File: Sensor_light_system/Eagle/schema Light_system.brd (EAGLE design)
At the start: 80.1 x 49.8 mm, 17 parts, among them IC1 STM32F030C8T6TR, J1 12_WAY_CON

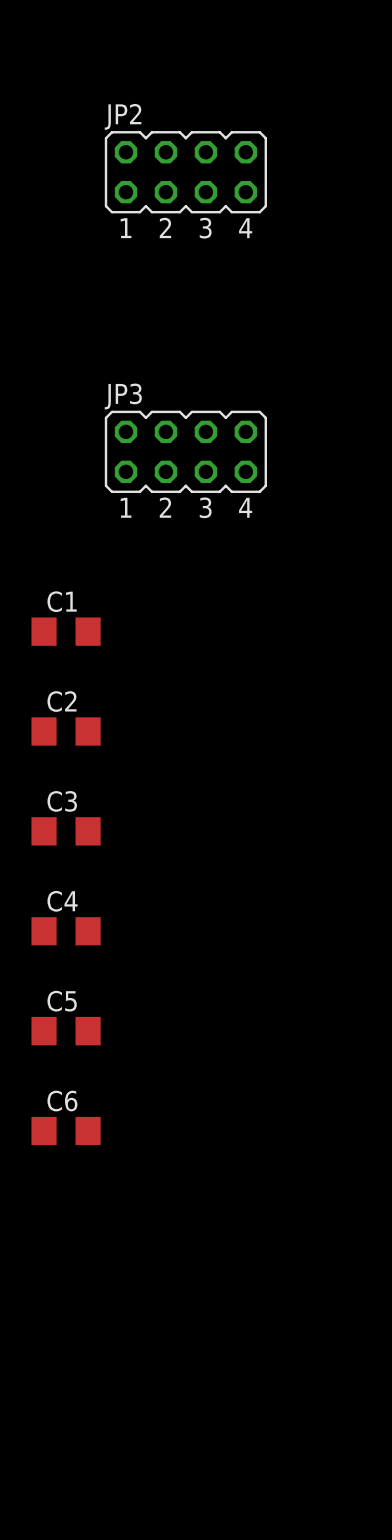
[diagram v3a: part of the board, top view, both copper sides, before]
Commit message: schema sensor gewijzigd
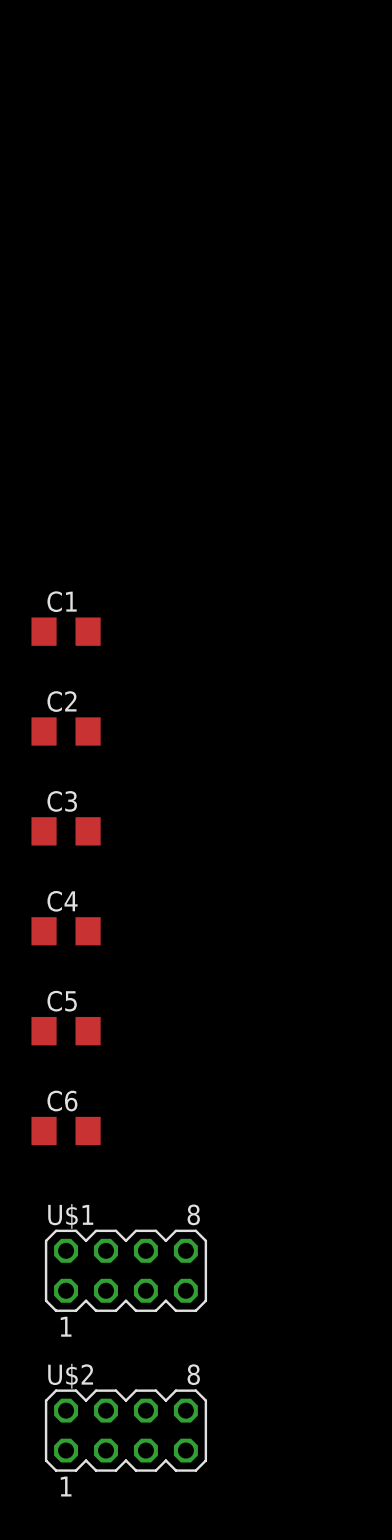
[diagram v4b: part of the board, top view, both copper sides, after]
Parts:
- removed JP2, JP3: (no value), jumper:JP4Q
- added U$1, U$2: MODULARCONNECTOR, Main_lib:MA04-2
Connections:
- net +3V3: no longer JP2.1, JP3.1
- net GND: no longer JP2.8, JP3.8
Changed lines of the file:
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@@
 <?xml version="1.0" encoding="utf-8"?>
 <!DOCTYPE eagle SYSTEM "eagle.dtd">
-<eagle version="8.0.2">
+<eagle version="9.2.0">
 <drawing>
 <settings>
 <setting alwaysvectorfont="yes"/>
+<setting keepoldvectorfont="yes"/>
 <setting verticaltext="up"/>
 </settings>
@@
 <param name="dpMaxLengthDifference" value="10mm"/>
 <param name="dpGapFactor" value="2.5"/>
-<param name="checkGrid" value="0"/>
 <param name="checkAngle" value="0"/>
 <param name="checkFont" value="1"/>
 <param name="checkRestrict" value="1"/>
+<param name="checkStop" value="0"/>
+<param name="checkValues" value="0"/>
+<param name="checkNames" value="1"/>
+<param name="checkWireStubs" value="1"/>
+<param name="checkPolygonWidth" value="0"/>
 <param name="useDiameter" value="13"/>
 <param name="maxErrors" value="50"/>
@@
 <attribute name="VALUE" x="11.73" y="-31.72" size="1.27" layer="27" align="center"/>
 </element>
-<element name="JP1" library="jumper" package="JP4Q" value="" x="-13.97" y="-49.53"/>
-<element name="JP2" library="jumper" package="JP4Q" value="" x="-13.97" y="-67.31"/>
-<element name="JP3" library="jumper" package="JP4Q" value="" x="-13.97" y="-85.09"/>
-<element name="C1" library="resistor" package="C1206" value="100nF" x="-21.59" y="-96.52"/>
-<element name="C2" library="resistor" package="C1206" value="100nF" x="-21.59" y="-102.87"/>
-<element name="C3" library="resistor" package="C1206" value="100nF" x="-21.59" y="-109.22"/>
-<element name="C4" library="resistor" package="C1206" value="100nF" x="-21.59" y="-115.57"/>
-<element name="C5" library="resistor" package="C1206" value="100nF" x="-21.59" y="-121.92"/>
-<element name="C6" library="resistor" package="C1206" value="100nF" x="-21.59" y="-128.27"/>
+<element name="JP1" library="jumper" package="JP4Q" value="" x="-13.97" y="-49.53">
+<attribute name="NAME" x="-19.05" y="-46.482" size="1.27" layer="25" ratio="10"/>
+<attribute name="VALUE" x="-19.05" y="-55.245" size="1.27" layer="27" ratio="10"/>
+</element>
+<element name="C1" library="resistor" package="C1206" value="100nF" x="-21.59" y="-96.52">
+<attribute name="NAME" x="-22.86" y="-95.25" size="1.27" layer="25"/>
+<attribute name="VALUE" x="-22.86" y="-99.06" size="1.27" layer="27"/>
+</element>
+<element name="C2" library="resistor" package="C1206" value="100nF" x="-21.59" y="-102.87">
+<attribute name="NAME" x="-22.86" y="-101.6" size="1.27" layer="25"/>
+<attribute name="VALUE" x="-22.86" y="-105.41" size="1.27" layer="27"/>
+</element>
+<element name="C3" library="resistor" package="C1206" value="100nF" x="-21.59" y="-109.22">
+<attribute name="NAME" x="-22.86" y="-107.95" size="1.27" layer="25"/>
+<attribute name="VALUE" x="-22.86" y="-111.76" size="1.27" layer="27"/>
+</element>
+<element name="C4" library="resistor" package="C1206" value="100nF" x="-21.59" y="-115.57">
+<attribute name="NAME" x="-22.86" y="-114.3" size="1.27" layer="25"/>
+<attribute name="VALUE" x="-22.86" y="-118.11" size="1.27" layer="27"/>
+</element>
+<element name="C5" library="resistor" package="C1206" value="100nF" x="-21.59" y="-121.92">
+<attribute name="NAME" x="-22.86" y="-120.65" size="1.27" layer="25"/>
+<attribute name="VALUE" x="-22.86" y="-124.46" size="1.27" layer="27"/>
+</element>
+<element name="C6" library="resistor" package="C1206" value="100nF" x="-21.59" y="-128.27">
+<attribute name="NAME" x="-22.86" y="-127" size="1.27" layer="25"/>
+<attribute name="VALUE" x="-22.86" y="-130.81" size="1.27" layer="27"/>
+</element>
+<element name="U$1" library="Main_lib" package="MA04-2" value="MODULARCONNECTOR" x="-17.78" y="-137.16">
+<attribute name="NAME" x="-22.86" y="-134.239" size="1.27" layer="25" ratio="10"/>
+<attribute name="VALUE" x="-17.78" y="-141.351" size="1.27" layer="27" ratio="10"/>
+</element>
+<element name="U$2" library="Main_lib" package="MA04-2" value="MODULARCONNECTOR" x="-17.78" y="-147.32">
+<attribute name="NAME" x="-22.86" y="-144.399" size="1.27" layer="25" ratio="10"/>
+<attribute name="VALUE" x="-17.78" y="-151.511" size="1.27" layer="27" ratio="10"/>
+</element>
 </elements>
 <signals>
@@
 <contactref element="C4" pad="2"/>
 <contactref element="C3" pad="2"/>
-<contactref element="JP2" pad="1"/>
-<contactref element="JP3" pad="1"/>
 <wire x1="-20.19" y1="-121.92" x2="-20.19" y2="-128.27" width="0" layer="19" extent="1-1"/>
 <wire x1="-20.19" y1="-115.57" x2="-20.19" y2="-121.92" width="0" layer="19" extent="1-1"/>
 <wire x1="-20.19" y1="-109.22" x2="-20.19" y2="-115.57" width="0" layer="19" extent="1-1"/>
 <wire x1="-20.19" y1="-102.87" x2="-20.19" y2="-109.22" width="0" layer="19" extent="1-1"/>
-<wire x1="-17.78" y1="-86.36" x2="-20.19" y2="-102.87" width="0" layer="19" extent="1-1"/>
-<wire x1="-17.78" y1="-68.58" x2="-17.78" y2="-86.36" width="0" layer="19" extent="1-1"/>
-<wire x1="-17.78" y1="-50.8" x2="-17.78" y2="-68.58" width="0" layer="19" extent="1-1"/>
+<wire x1="-17.78" y1="-50.8" x2="-20.19" y2="-102.87" width="0" layer="19" extent="1-1"/>
 <wire x1="0.842" y1="-7.6" x2="-17.78" y2="-50.8" width="0" layer="19" extent="1-1"/>
 <wire x1="0.842" y1="-3.6" x2="0.842" y2="-7.6" width="0" layer="19" extent="1-1"/>
@@
 <contactref element="C6" pad="1"/>
 <contactref element="C3" pad="1"/>
-<contactref element="JP2" pad="8"/>
-<contactref element="JP3" pad="8"/>
 <wire x1="-22.99" y1="-121.92" x2="-22.99" y2="-128.27" width="0" layer="19" extent="1-1"/>
 <wire x1="-22.99" y1="-115.57" x2="-22.99" y2="-121.92" width="0" layer="19" extent="1-1"/>
@@
 <wire x1="-22.99" y1="-102.87" x2="-22.99" y2="-109.22" width="0" layer="19" extent="1-1"/>
 <wire x1="-22.99" y1="-96.52" x2="-22.99" y2="-102.87" width="0" layer="19" extent="1-1"/>
-<wire x1="-10.16" y1="-83.82" x2="-22.99" y2="-96.52" width="0" layer="19" extent="1-1"/>
-<wire x1="-10.16" y1="-66.04" x2="-10.16" y2="-83.82" width="0" layer="19" extent="1-1"/>
-<wire x1="-10.16" y1="-48.26" x2="-10.16" y2="-66.04" width="0" layer="19" extent="1-1"/>
+<wire x1="-10.16" y1="-48.26" x2="-22.99" y2="-96.52" width="0" layer="19" extent="1-1"/>
 <wire x1="-1.73" y1="-18.07" x2="-10.16" y2="-48.26" width="0" layer="19" extent="1-1"/>
 <wire x1="4.27" y1="-18.07" x2="-1.73" y2="-18.07" width="0" layer="19" extent="1-1"/>
@@
 </signal>
 </signals>
+<mfgpreviewcolors>
+<mfgpreviewcolor name="soldermaskcolor" color="0xC8008000"/>
+<mfgpreviewcolor name="silkscreencolor" color="0xFFFEFEFE"/>
+<mfgpreviewcolor name="backgroundcolor" color="0xFF282828"/>
+<mfgpreviewcolor name="coppercolor" color="0xFFFFBF00"/>
+<mfgpreviewcolor name="substratecolor" color="0xFF786E46"/>
+</mfgpreviewcolors>
 </board>
 </drawing>
+<compatibility>
+<note version="8.3" severity="warning">
+Since Version 8.3, EAGLE supports URNs for individual library
+assets (packages, symbols, and devices). The URNs of those assets
+will not be understood (or retained) with this version.
+</note>
+</compatibility>
 </eagle>

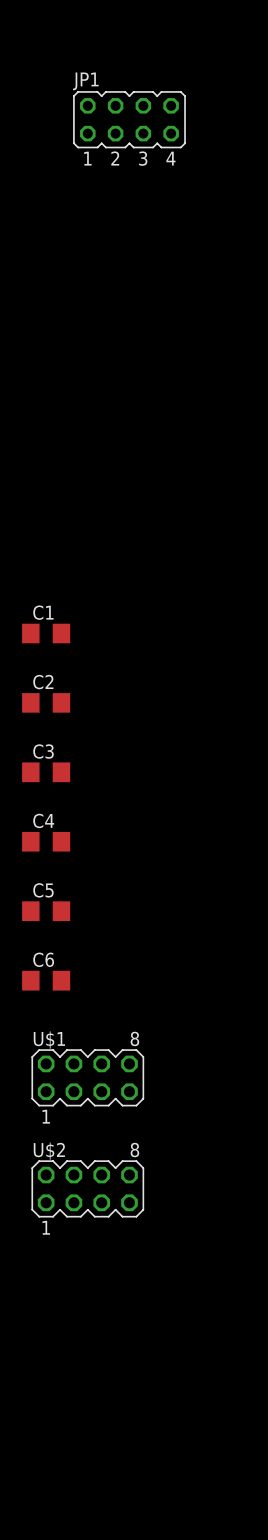
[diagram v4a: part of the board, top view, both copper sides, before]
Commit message: schema sensor gewijzigd
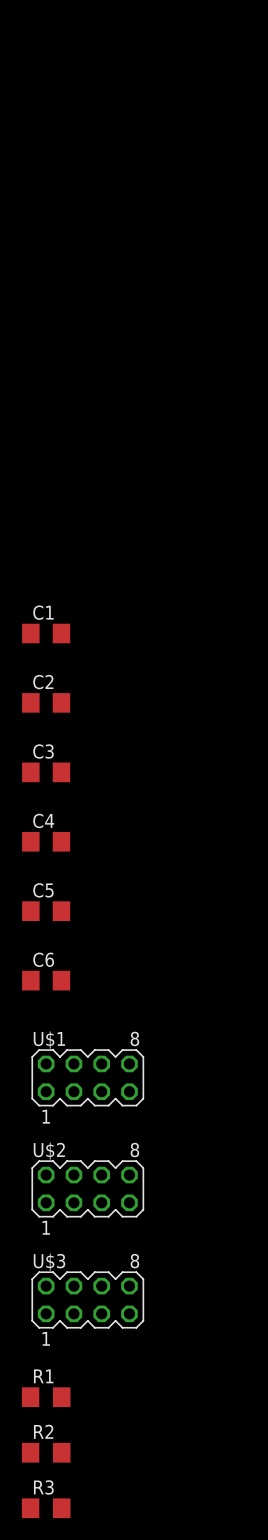
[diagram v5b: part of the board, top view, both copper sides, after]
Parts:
- removed JP1: (no value), jumper:JP4Q
- added R1, R2, R3: 1K, rcl:R1206
- added U$3: MODULARCONNECTOR, Main_lib:MA04-2
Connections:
- new net I2C1_SCL: IC1.42, U$1.6, U$2.6
- new net I2C1_SDA: IC1.43, U$1.5, U$2.5
- new net N$1: LED1.2, R1.1
- new net N$2: LED1.3, R2.1
- new net N$4: LED1.4, R3.1
- new net N$5: U$1.1, U$2.1
- new net N$6: U$1.2, U$2.2
- new net N$7: IC1.19, R2.2
- new net N$8: IC1.20, R3.2
- new net N$9: IC1.18, R1.2
- new net PA0: IC1.10, J1.3
- new net PA1: IC1.11, J1.4
- new net PA2: IC1.12, J1.5
- new net PA3: IC1.13, J1.6
- new net PA4: IC1.14, J1.7
- new net PA5: IC1.15, J1.8
- new net PA6: IC1.16, J1.9
- new net PA7: IC1.17, J1.10
- new net PA8: IC1.29, J1.11
- new net PA9: IC1.30, J1.12
- new net RST: U$3.1
- new net SWCLK: U$3.2
- new net SWDIO: U$3.4
- new net SWIM: U$3.3
- net +3V3: now also J1.1, LED1.1, U$1.3, U$1.4, U$2.3, U$2.4, U$3.7, U$3.8; no longer JP1.1
- net GND: now also J1.2, U$1.7, U$1.8, U$2.7, U$2.8, U$3.5, U$3.6; no longer JP1.8

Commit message: schema Light_system
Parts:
- added C7: 100nF, resistor:C1206
- added C8: 10nF, resistor:C1206
- added D1: BAT60J, diode:SOD323_ST
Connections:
- removed net N$3: C1.2, IC1.7, S1.3, S1.4
- net +3V3: now also C7.2, C8.2, D1.A, D1.C
- net GND: now also C7.1, C8.1
- net RST: now also C1.2, IC1.7, S1.3, S1.4
- net SWCLK: now also IC1.37
- net SWDIO: now also IC1.34

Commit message: board aangepast
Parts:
- moved D1 243.8 mm to (55.9, 35.6), turned to 90 degrees
- moved C8 229.9 mm to (41.9, 31.8), turned to 90 degrees
- moved C7 222.8 mm to (38.1, 31.8), turned to 90 degrees
- moved U$3 204.8 mm to (16.5, 44.5)
- moved R3 200.4 mm to (44.5, 12.7), turned to 90 degrees
- moved R2 197.0 mm to (48.3, 12.7), turned to 90 degrees
- moved R1 193.6 mm to (52.1, 12.7), turned to 90 degrees
- moved U$2 187.8 mm to (56.9, 25.0), flipped to the bottom, turned to 90 degrees
- moved C3 165.8 mm to (40.6, 44.5), turned to 90 degrees
- moved U$1 163.5 mm to (3.10, 25.0), turned to 90 degrees
- moved C6 163.2 mm to (36.8, 24.1), turned to 90 degrees
- moved C5 159.3 mm to (41.9, 24.1), turned to 90 degrees
- moved C2 157.6 mm to (34.3, 44.5), turned to 90 degrees
- moved C4 155.1 mm to (45.7, 24.1), turned to 90 degrees
- moved C1 137.4 mm to (11.4, 36.8), turned to 270 degrees
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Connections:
- removed net N$6: U$1.2, U$2.2
- net N$5: now also U$1.2, U$2.2
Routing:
- net +3V3: track 0.00 -> 86.0 mm
- net GND: track 0.00 -> 85.5 mm
- net I2C1_SCL: track 0.00 -> 57.5 mm
- net N$5: track 0.00 -> 56.3 mm
- net I2C1_SDA: track 0.00 -> 51.8 mm
- net SWDIO: track 0.00 -> 34.6 mm
- net PA8: track 0.00 -> 23.2 mm
- net SWCLK: track 0.00 -> 22.4 mm
- net PA0: track 0.00 -> 20.1 mm
- net PA9: track 0.00 -> 20.0 mm
- net RST: track 0.00 -> 19.7 mm
- net PA6: track 0.00 -> 19.5 mm
- net PA2: track 0.00 -> 17.6 mm
- net PA4: track 0.00 -> 17.2 mm
- net PA7: track 0.00 -> 16.6 mm
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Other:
- board size 80.1 x 49.8 mm -> 60 x 50 mm

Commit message: eagle
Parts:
- moved D1 39.1 mm to (17.8, 26.7)
- moved C8 27.7 mm to (15.2, 24.1), turned to 270 degrees
- moved C7 17.8 mm to (20.3, 33.0), turned to 180 degrees
- moved C3 14.0 mm to (26.7, 44.5)
- moved C2 10.2 mm to (24.1, 44.5)
- moved C4 2.84 mm to (47.0, 26.7), turned to 270 degrees
- moved C5 2.54 mm to (41.9, 26.7), turned to 270 degrees
- moved C6 2.54 mm to (36.8, 26.7), turned to 270 degrees
- moved R2 1.80 mm to (47.0, 14.0)
- moved R3 1.27 mm to (44.5, 14.0)
- moved R1 1.27 mm to (52.1, 11.4), turned to 270 degrees
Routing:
- net GND: track 85.5 -> 167.5 mm, vias 0 -> 4
- net +3V3: track 86.0 -> 160.2 mm, vias 0 -> 3
- net N$9: track 0.00 -> 38.7 mm
- net N$7: track 0.00 -> 27.2 mm
- net N$8: track 0.00 -> 23.5 mm
- net RST: track 19.7 -> 37.3 mm
- net SWCLK: track 22.4 -> 37.2 mm
- net SWDIO: track 34.6 -> 40.8 mm
- net I2C1_SCL: track 57.5 -> 62.5 mm, vias 0 -> 1
- net I2C1_SDA: track 51.8 -> 55.1 mm, vias 0 -> 1
- net N$4: track 5.55 -> 6.82 mm
- net N$1: track 5.45 -> 6.36 mm
- net N$2: track 3.96 -> 4.70 mm
- net PA7: track 16.6 -> 17.3 mm
- net PA6: track 19.5 -> 20.3 mm
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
